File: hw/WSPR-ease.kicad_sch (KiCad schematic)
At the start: 55 parts, among them J101 SMA, J102 SMA, J103 pwr+data, Q101 MMBF170, U101 GNSS module, U102 ESP32-S3-WROOM-1-N8R8, U103 SRV05-4, U104 TPS74612PQWDRBRQ1, U105 TPS22918DBVR, U106 LMR51430YDDCR

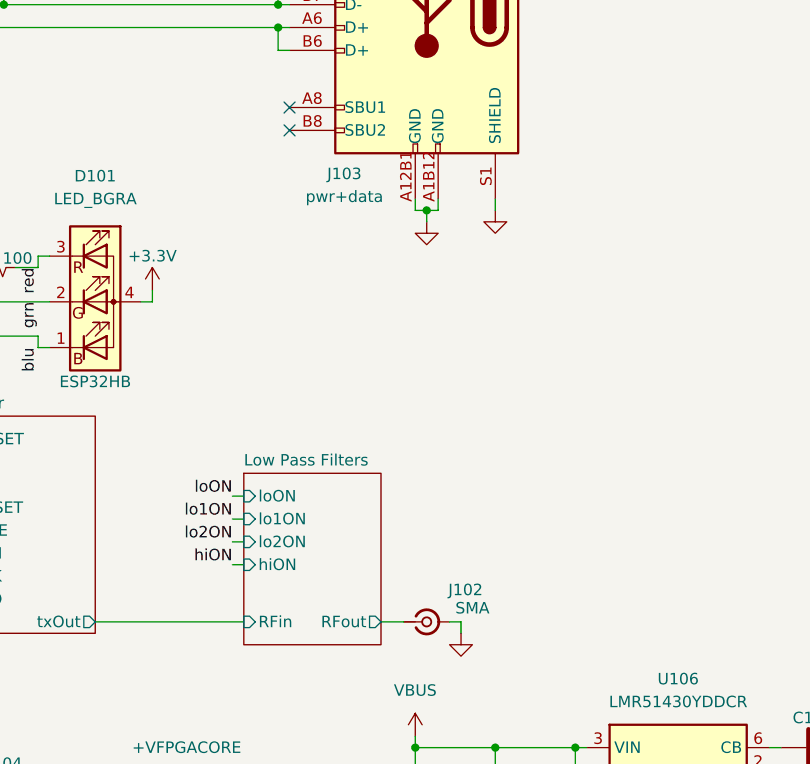
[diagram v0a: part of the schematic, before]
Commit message: Move to single gate buffer per MOSFET to distribute decoupling and gate drive across more devices and improve gate drive signal quality at high speed
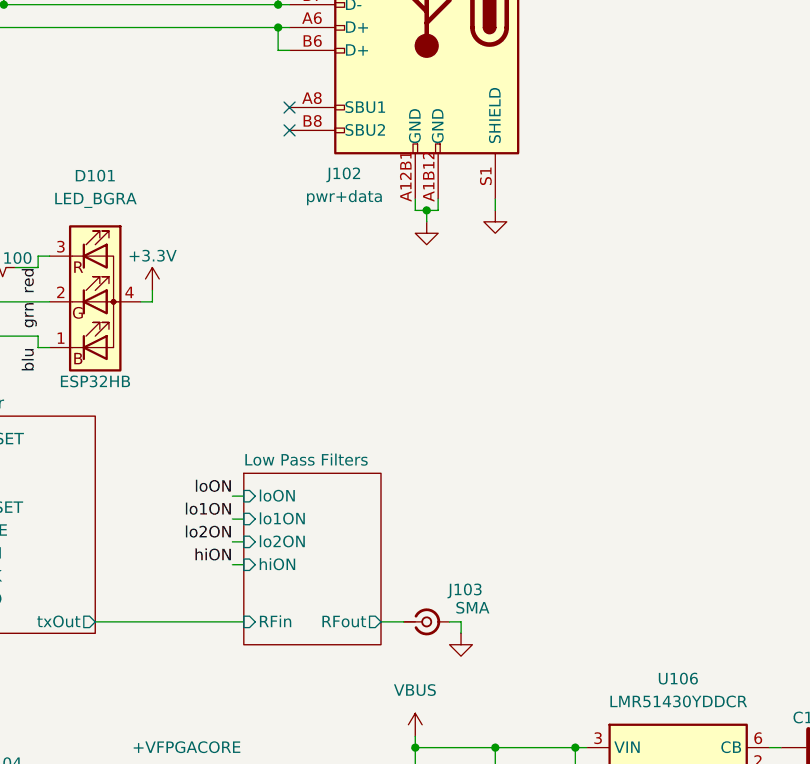
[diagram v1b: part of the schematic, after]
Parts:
- renumbered J103 to J102, J102 to J103
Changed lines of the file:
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@@
 		(dnp no)
 		(fields_autoplaced yes)
-		(property "Reference" "#PWR0133"
+		(property "Reference" "#PWR0132"
 			(at 170.18 148.59 0)
 			(effects
@@
 			(project "WSPR-ease"
 				(path "/31075357-d7d2-474d-bd47-511c83e129b3"
-					(reference "#PWR0133")
+					(reference "#PWR0132")
 					(unit 1)
 				)
@@
 		(on_board yes)
 		(dnp no)
-		(property "Reference" "#PWR0135"
+		(property "Reference" "#PWR0134"
 			(at 171.45 93.98 0)
 			(effects
@@
 			(project "WSPR-ease"
 				(path "/31075357-d7d2-474d-bd47-511c83e129b3"
-					(reference "#PWR0135")
+					(reference "#PWR0134")
 					(unit 1)
 				)
@@
 		(dnp no)
 		(fields_autoplaced yes)
-		(property "Reference" "#PWR0136"
+		(property "Reference" "#PWR0135"
 			(at 175.26 33.02 0)
 			(effects
@@
 			(project "WSPR-ease"
 				(path "/31075357-d7d2-474d-bd47-511c83e129b3"
-					(reference "#PWR0136")
+					(reference "#PWR0135")
 					(unit 1)
 				)
@@
 		(dnp no)
 		(fields_autoplaced yes)
-		(property "Reference" "#PWR0134"
+		(property "Reference" "#PWR0133"
 			(at 170.18 165.1 0)
 			(effects
@@
 			(project "WSPR-ease"
 				(path "/31075357-d7d2-474d-bd47-511c83e129b3"
-					(reference "#PWR0134")
+					(reference "#PWR0133")
 					(unit 1)
 				)
@@
 		(dnp no)
 		(fields_autoplaced yes)
-		(property "Reference" "#PWR0132"
+		(property "Reference" "#PWR0136"
 			(at 175.26 139.7 0)
 			(effects
@@
 			(project "WSPR-ease"
 				(path "/31075357-d7d2-474d-bd47-511c83e129b3"
-					(reference "#PWR0132")
+					(reference "#PWR0136")
 					(unit 1)
 				)
@@
 		(on_board yes)
 		(dnp no)
-		(property "Reference" "J103"
+		(property "Reference" "J102"
 			(at 162.306 82.296 0)
 			(effects
@@
 			(project "WSPR-ease"
 				(path "/31075357-d7d2-474d-bd47-511c83e129b3"
-					(reference "J103")
+					(reference "J102")
 					(unit 1)
 				)
@@
 		(on_board yes)
 		(dnp no)
-		(property "Reference" "J102"
+		(property "Reference" "J103"
 			(at 175.768 128.524 0)
 			(effects
@@
 			(project "WSPR-ease"
 				(path "/31075357-d7d2-474d-bd47-511c83e129b3"
-					(reference "J102")
+					(reference "J103")
 					(unit 1)
 				)
